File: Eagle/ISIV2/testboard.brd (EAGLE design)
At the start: 71.8 x 43.9 mm, 18 parts, among them IC1 74ALS04D, U1 LTC6905CS5TRMPBF

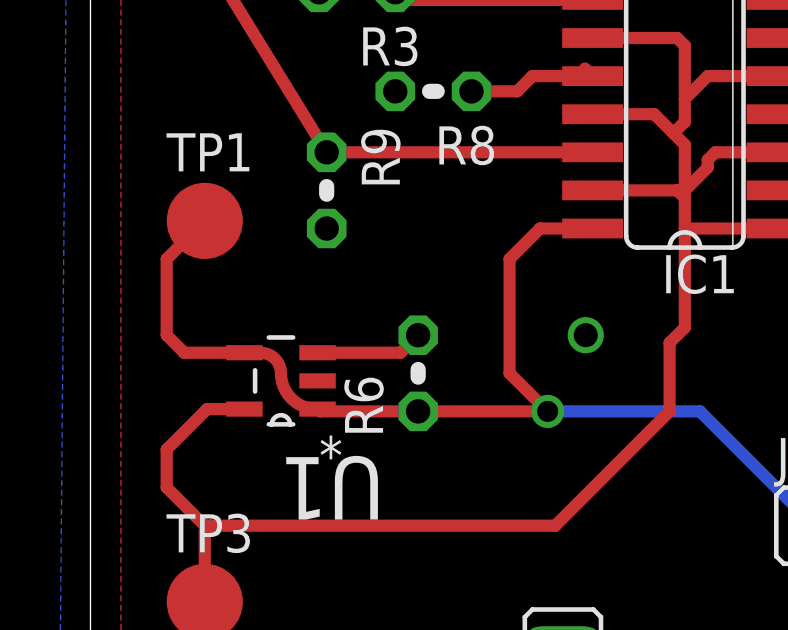
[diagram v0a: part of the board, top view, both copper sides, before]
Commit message: WPRs and Test Board
Test board layout
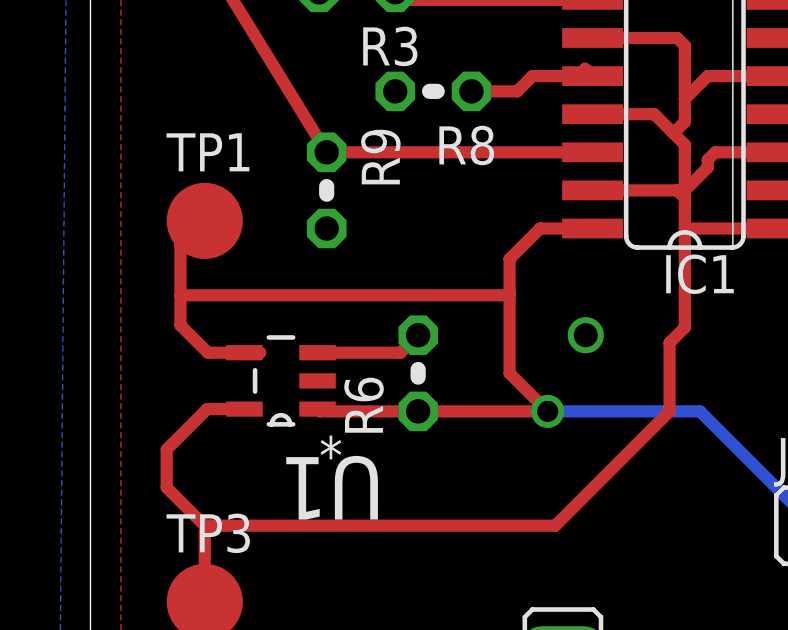
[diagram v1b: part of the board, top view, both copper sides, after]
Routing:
- net VCC: track 37.4 -> 44.8 mm
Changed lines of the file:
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@@
 <?xml version="1.0" encoding="utf-8"?>
 <!DOCTYPE eagle SYSTEM "eagle.dtd">
-<eagle version="7.2.0">
+<eagle version="7.1.0">
 <drawing>
 <settings>
@@
 <wire x1="7.6454" y1="24.13" x2="10.922" y2="24.13" width="0.4064" layer="1"/>
 <wire x1="5.1308" y1="26.0858" x2="5.6642" y2="26.0858" width="0.4064" layer="1"/>
-<wire x1="5.6642" y1="26.0858" x2="6.35" y2="25.4" width="0.4064" layer="1" curve="-90"/>
-<wire x1="6.35" y1="25.4" x2="7.5438" y2="24.2062" width="0.4064" layer="1" curve="90"/>
 <wire x1="7.5438" y1="24.2062" x2="7.5692" y2="24.2062" width="0.4064" layer="1"/>
 <wire x1="10.922" y1="24.13" x2="15.24" y2="24.13" width="0.4064" layer="1"/>
@@
 <wire x1="16.7386" y1="30.226" x2="14.986" y2="30.226" width="0.4064" layer="1"/>
 <wire x1="14.986" y1="30.226" x2="13.97" y2="29.21" width="0.4064" layer="1"/>
-<wire x1="13.97" y1="29.21" x2="13.97" y2="25.4" width="0.4064" layer="1"/>
+<wire x1="13.97" y1="29.21" x2="13.97" y2="28" width="0.4064" layer="1"/>
+<wire x1="13.97" y1="28" x2="13.97" y2="25.4" width="0.4064" layer="1"/>
 <wire x1="13.97" y1="25.4" x2="15.24" y2="24.13" width="0.4064" layer="1"/>
 <contactref element="JP1" pad="1"/>
@@
 <wire x1="24.13" y1="20.32" x2="20.32" y2="24.13" width="0.4064" layer="16"/>
 <wire x1="20.32" y1="24.13" x2="15.24" y2="24.13" width="0.4064" layer="16"/>
-<wire x1="5.1308" y1="26.0858" x2="3.1242" y2="26.0858" width="0.4064" layer="1"/>
-<wire x1="3.1242" y1="26.0858" x2="2.54" y2="26.67" width="0.4064" layer="1"/>
-<wire x1="2.54" y1="26.67" x2="2.54" y2="29.21" width="0.4064" layer="1"/>
-<wire x1="2.54" y1="29.21" x2="3.81" y2="30.48" width="0.4064" layer="1"/>
+<wire x1="5.1308" y1="26.0858" x2="3.9142" y2="26.0858" width="0.4064" layer="1"/>
+<wire x1="3" y1="28" x2="13.97" y2="28" width="0.4064" layer="1"/>
+<wire x1="3" y1="29.67" x2="3.81" y2="30.48" width="0.4064" layer="1"/>
+<wire x1="3.9142" y1="26.0858" x2="3" y2="27" width="0.4064" layer="1"/>
+<wire x1="3" y1="27" x2="3" y2="29.67" width="0.4064" layer="1"/>
+<wire x1="3" y1="27" x2="3" y2="28" width="0" layer="19" extent="1-1"/>
 </signal>
 <signal name="N$4">
